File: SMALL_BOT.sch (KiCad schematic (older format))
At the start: 37 parts, among them J1 MOTOR_B, J10 JMP, J11 UART, J12 LEDS, J13 I2C, J14 LEDS, J15 HEADER_1, J16 HEADER_1, J2 MOTOR_A, J3 HEADER_1, J4 HEADER_1, J5 HC-SR04, J6 HC-SR04, J7 HC-SR04, J8 HC-SR04, J9 Bateria, Q1 2N7002, U1 Teensy4.0_B, U2 DRV8872, U3 LM1117-SOT, U4 DRV8872

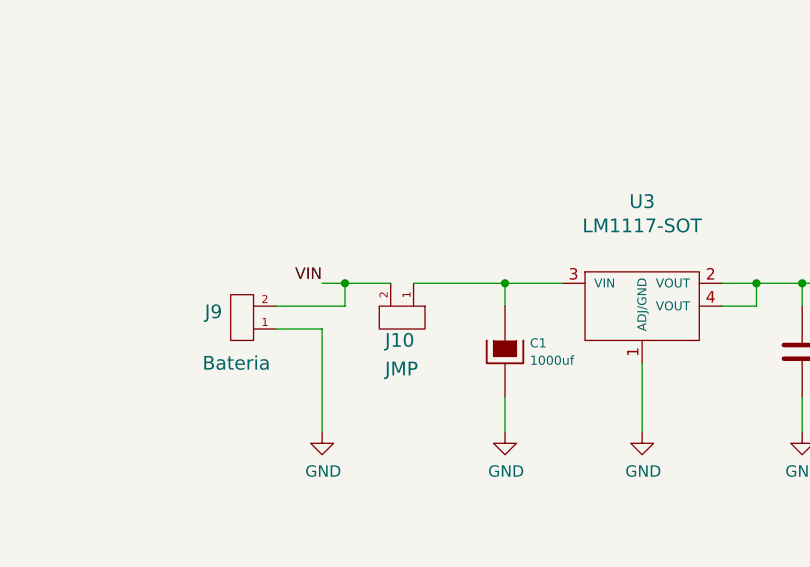
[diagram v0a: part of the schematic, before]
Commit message: SCH y capacitores
Genera la version inicial del SCH en pdf y  cambie de posición 2 capacitores SMD que estaban debajo de uno de los motores.
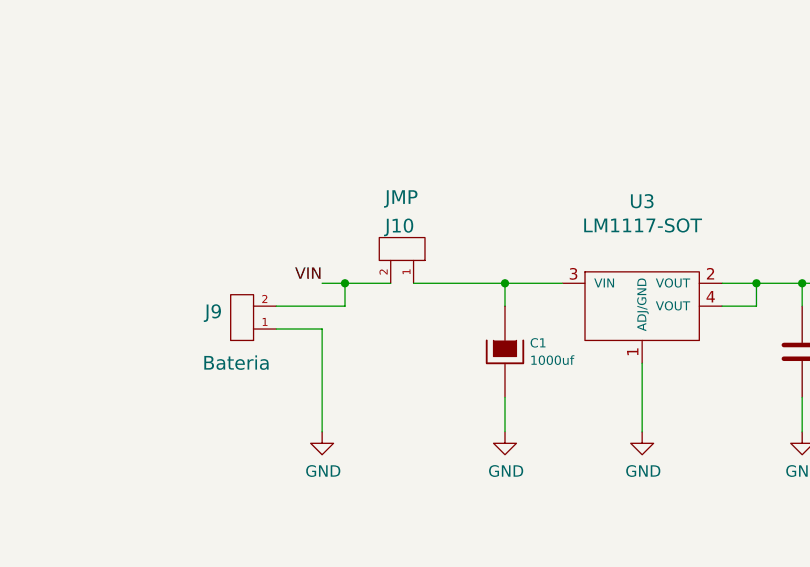
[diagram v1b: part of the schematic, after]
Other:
- moved on the sheet: J10
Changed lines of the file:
@@
 EESchema Schematic File Version 4
-LIBS:SMALL_BOT-cache
 EELAYER 30 0
 EELAYER END
@@
 Wire Wire Line
 	7600 5550 7900 5550
-$Comp
-L EESTN5:HEADER_2 J10
-U 1 1 5FD52493
-P 8150 5550
-F 0 "J10" V 8300 5475 60  0000 L CNN
-F 1 "JMP" V 8425 5475 60  0000 L CNN
-F 2 "EESTN5:Pin_strip_2" H 8150 5800 60  0001 C CNN
-F 3 "" H 8150 5800 60  0000 C CNN
-	1    8150 5550
-	0    1    1    0
-$EndComp
 Wire Wire Line
 	8200 5450 8600 5450
@@
 Wire Notes Line
 	3850 950  5400 950
+$Comp
+L EESTN5:HEADER_2 J10
+U 1 1 5FD52493
+P 8150 5350
+F 0 "J10" V 8300 5275 60  0000 L CNN
+F 1 "JMP" V 8425 5275 60  0000 L CNN
+F 2 "EESTN5:Pin_strip_2" H 8150 5600 60  0001 C CNN
+F 3 "" H 8150 5600 60  0000 C CNN
+	1    8150 5350
+	0    1    -1   0
+$EndComp
 $EndSCHEMATC

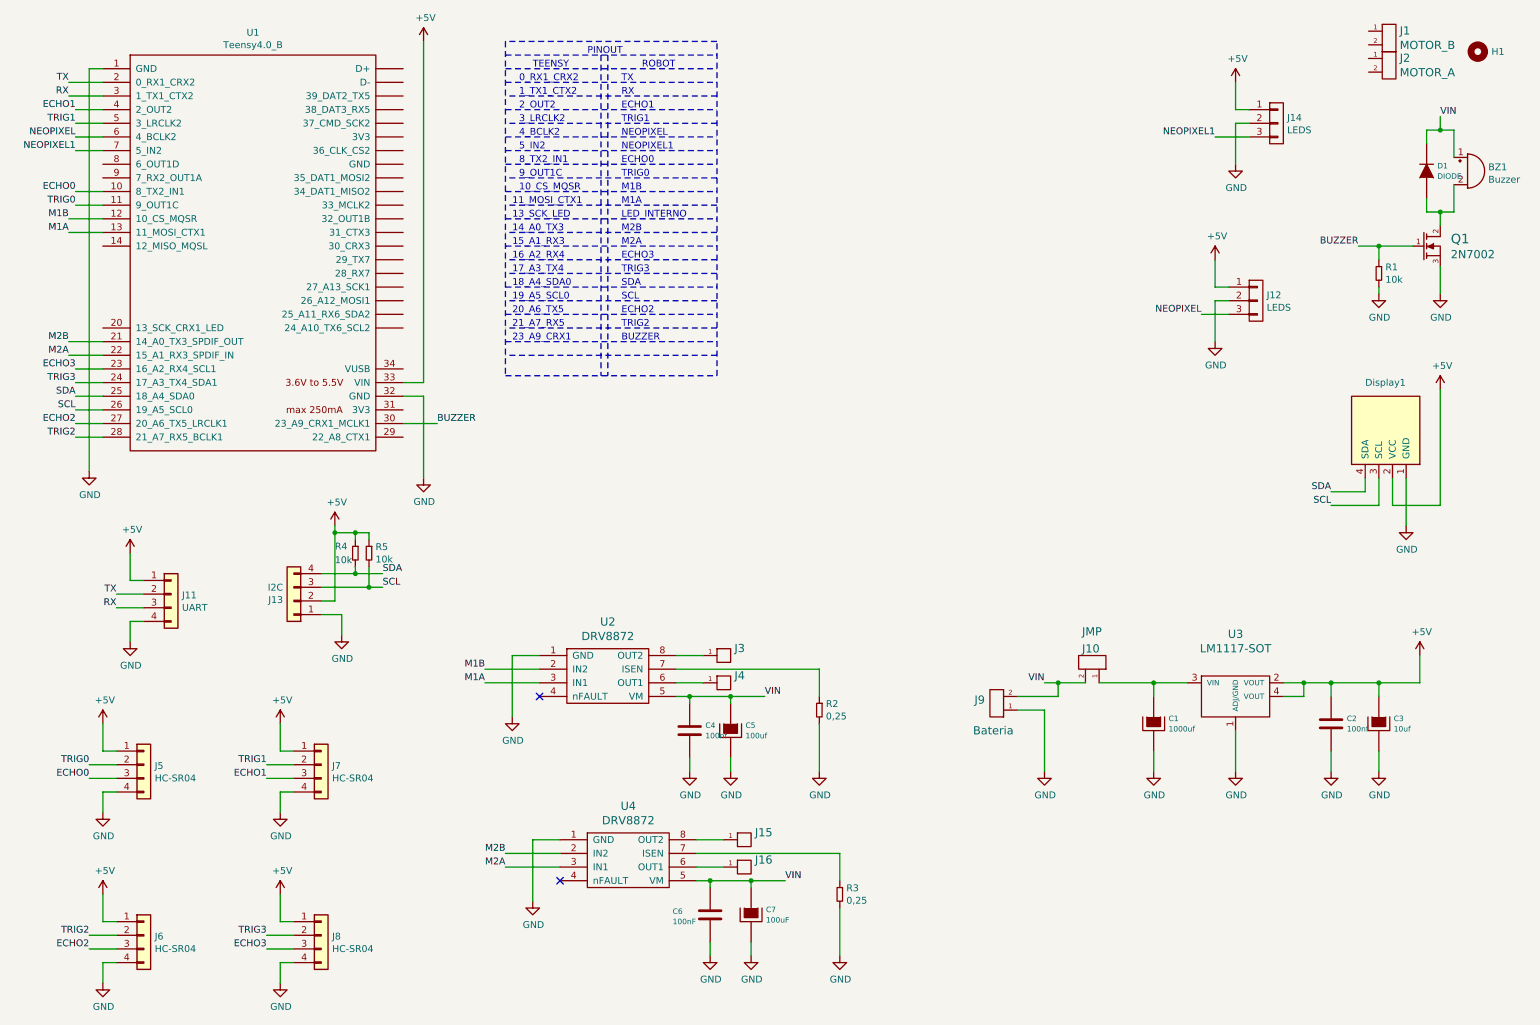
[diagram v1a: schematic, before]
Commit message: Comentarios en SCH
Deje algunos comentarios para hacer cambios en el sch para contemplar que la teensy no es tolerante a 5V y las conexiones de los perisfericos deben tener en cuenta ésto.
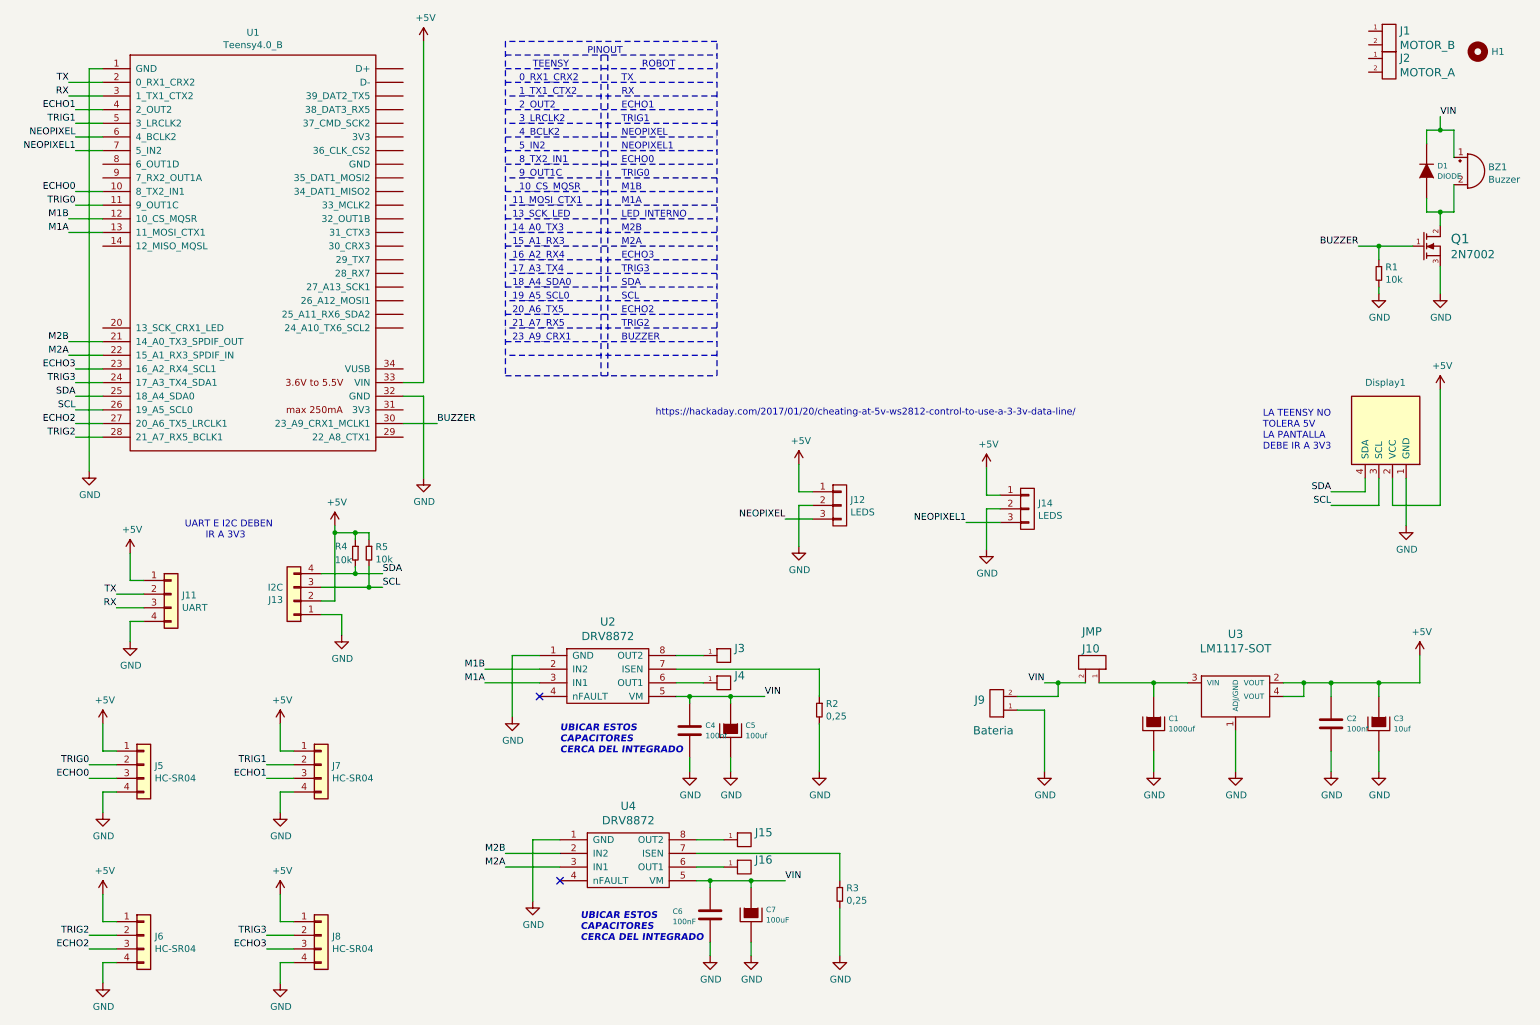
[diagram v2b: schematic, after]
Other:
- note added: "LA TEENSY NO\nTOLERA 5V\nLA PANTALLA\nDEBE IR A 3V3"
- note added: "UART E I2C DEBEN \n IR A 3V3"
- note added: "UBICAR ESTOS\nCAPACITORES\nCERCA DEL INTEGRADO"
- note added: "https://hackaday.com/2017/01/20/cheating-at-5v-ws2812-control-to-use-a-3-3v-data-line/"
- moved on the sheet: J12, J14
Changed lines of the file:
@@
 L EESTN5:Conn_01X03 J12
 U 1 1 5FD97C02
-P 9350 2650
-F 0 "J12" H 9428 2691 50  0000 L CNN
-F 1 "LEDS" H 9428 2600 50  0000 L CNN
-F 2 "EESTN5:Pin_Strip_3" H 9350 2650 50  0001 C CNN
-F 3 "" H 9350 2650 50  0001 C CNN
-	1    9350 2650
-	1    0    0    -1
-$EndComp
-Wire Wire Line
-	9150 2550 9050 2550
-Wire Wire Line
-	9050 2550 9050 2350
+P 6300 4150
+F 0 "J12" H 6378 4191 50  0000 L CNN
+F 1 "LEDS" H 6378 4100 50  0000 L CNN
+F 2 "EESTN5:Pin_Strip_3" H 6300 4150 50  0001 C CNN
+F 3 "" H 6300 4150 50  0001 C CNN
+	1    6300 4150
+	1    0    0    -1
+$EndComp
+Wire Wire Line
+	6100 4050 6000 4050
+Wire Wire Line
+	6000 4050 6000 3850
 $Comp
 L power:+5V #PWR0124
 U 1 1 5FD9C4FB
-P 9050 2350
-F 0 "#PWR0124" H 9050 2200 50  0001 C CNN
-F 1 "+5V" H 9065 2523 50  0000 C CNN
-F 2 "" H 9050 2350 50  0001 C CNN
-F 3 "" H 9050 2350 50  0001 C CNN
-	1    9050 2350
-	1    0    0    -1
-$EndComp
-Wire Wire Line
-	9150 2650 9050 2650
-Text Label 8950 2750 2    50   ~ 0
+P 6000 3850
+F 0 "#PWR0124" H 6000 3700 50  0001 C CNN
+F 1 "+5V" H 6015 4023 50  0000 C CNN
+F 2 "" H 6000 3850 50  0001 C CNN
+F 3 "" H 6000 3850 50  0001 C CNN
+	1    6000 3850
+	1    0    0    -1
+$EndComp
+Wire Wire Line
+	6100 4150 6000 4150
+Text Label 5900 4250 2    50   ~ 0
 NEOPIXEL
 $Comp
 L power:GND #PWR0125
 U 1 1 5FDA4254
-P 9050 2950
-F 0 "#PWR0125" H 9050 2700 50  0001 C CNN
-F 1 "GND" H 9055 2777 50  0000 C CNN
-F 2 "" H 9050 2950 50  0001 C CNN
-F 3 "" H 9050 2950 50  0001 C CNN
-	1    9050 2950
+P 6000 4450
+F 0 "#PWR0125" H 6000 4200 50  0001 C CNN
+F 1 "GND" H 6005 4277 50  0000 C CNN
+F 2 "" H 6000 4450 50  0001 C CNN
+F 3 "" H 6000 4450 50  0001 C CNN
+	1    6000 4450
 	1    0    0    -1
 $EndComp
@@
 L EESTN5:Conn_01X03 J14
 U 1 1 5FE32101
-P 9500 1350
-F 0 "J14" H 9578 1391 50  0000 L CNN
-F 1 "LEDS" H 9578 1300 50  0000 L CNN
-F 2 "EESTN5:Pin_Strip_3" H 9500 1350 50  0001 C CNN
-F 3 "" H 9500 1350 50  0001 C CNN
-	1    9500 1350
-	1    0    0    -1
-$EndComp
-Wire Wire Line
-	9300 1250 9200 1250
-Wire Wire Line
-	9200 1250 9200 1050
+P 7675 4175
+F 0 "J14" H 7753 4216 50  0000 L CNN
+F 1 "LEDS" H 7753 4125 50  0000 L CNN
+F 2 "EESTN5:Pin_Strip_3" H 7675 4175 50  0001 C CNN
+F 3 "" H 7675 4175 50  0001 C CNN
+	1    7675 4175
+	1    0    0    -1
+$EndComp
+Wire Wire Line
+	7475 4075 7375 4075
+Wire Wire Line
+	7375 4075 7375 3875
 $Comp
 L power:+5V #PWR0128
 U 1 1 5FE32289
-P 9200 1050
-F 0 "#PWR0128" H 9200 900 50  0001 C CNN
-F 1 "+5V" H 9215 1223 50  0000 C CNN
-F 2 "" H 9200 1050 50  0001 C CNN
-F 3 "" H 9200 1050 50  0001 C CNN
-	1    9200 1050
-	1    0    0    -1
-$EndComp
-Text Label 9050 1450 2    50   ~ 0
+P 7375 3875
+F 0 "#PWR0128" H 7375 3725 50  0001 C CNN
+F 1 "+5V" H 7390 4048 50  0000 C CNN
+F 2 "" H 7375 3875 50  0001 C CNN
+F 3 "" H 7375 3875 50  0001 C CNN
+	1    7375 3875
+	1    0    0    -1
+$EndComp
+Text Label 7225 4275 2    50   ~ 0
 NEOPIXEL1
 $Comp
 L power:GND #PWR0129
 U 1 1 5FE32297
-P 9200 1650
-F 0 "#PWR0129" H 9200 1400 50  0001 C CNN
-F 1 "GND" H 9205 1477 50  0000 C CNN
-F 2 "" H 9200 1650 50  0001 C CNN
-F 3 "" H 9200 1650 50  0001 C CNN
-	1    9200 1650
+P 7375 4475
+F 0 "#PWR0129" H 7375 4225 50  0001 C CNN
+F 1 "GND" H 7380 4302 50  0000 C CNN
+F 2 "" H 7375 4475 50  0001 C CNN
+F 3 "" H 7375 4475 50  0001 C CNN
+	1    7375 4475
 	1    0    0    -1
 $EndComp
@@
 M2B
 Wire Wire Line
-	9050 2650 9050 2950
-Wire Wire Line
-	8950 2750 9150 2750
-Wire Wire Line
-	9200 1350 9300 1350
-Wire Wire Line
-	9200 1350 9200 1650
-Wire Wire Line
-	9300 1450 9050 1450
+	6000 4150 6000 4450
+Wire Wire Line
+	5900 4250 6100 4250
+Wire Wire Line
+	7375 4175 7475 4175
+Wire Wire Line
+	7375 4175 7375 4475
+Wire Wire Line
+	7475 4275 7225 4275
 $Comp
 L EESTN5:R R4
@@
 	0    1    -1   0
 $EndComp
+Text Notes 4250 5975 0    50   Italic 10
+UBICAR ESTOS\nCAPACITORES\nCERCA DEL INTEGRADO
+Text Notes 4400 7350 0    50   Italic 10
+UBICAR ESTOS\nCAPACITORES\nCERCA DEL INTEGRADO
+Text Notes 9400 3750 0    50   ~ 0
+LA TEENSY NO\nTOLERA 5V\nLA PANTALLA\nDEBE IR A 3V3
+Text Notes 4950 3500 0    50   ~ 0
+https://hackaday.com/2017/01/20/cheating-at-5v-ws2812-control-to-use-a-3-3v-data-line/
+Text Notes 1500 4400 0    50   ~ 0
+UART E I2C DEBEN \n       IR A 3V3
 $EndSCHEMATC
